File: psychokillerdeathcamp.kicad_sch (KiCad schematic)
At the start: 0 parts

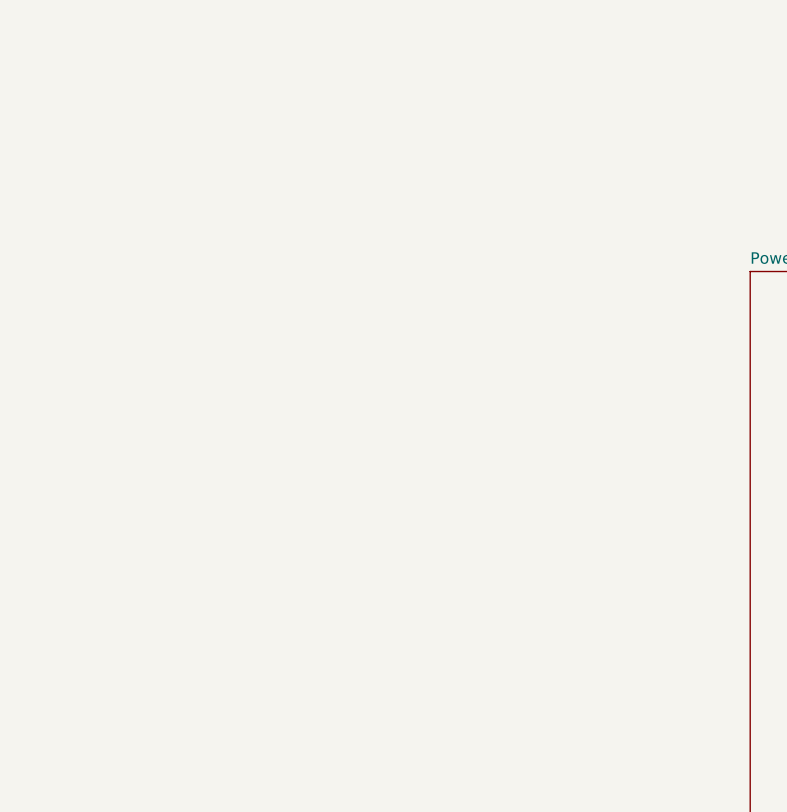
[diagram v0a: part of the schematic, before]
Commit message: fpga not done
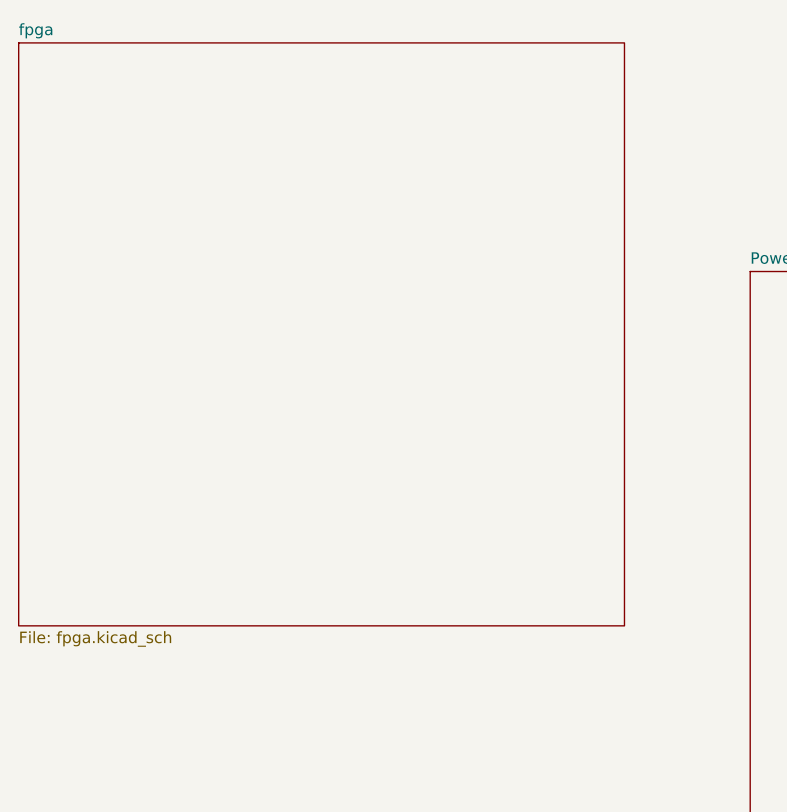
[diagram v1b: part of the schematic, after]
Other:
- added sheet fpga (fpga.kicad_sch)
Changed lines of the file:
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@@
+		)
+	)
+	(sheet
+		(at 19.05 38.1)
+		(size 67.31 64.77)
+		(exclude_from_sim no)
+		(in_bom yes)
+		(on_board yes)
+		(dnp no)
+		(fields_autoplaced yes)
+		(stroke
+			(width 0.1524)
+			(type solid)
+		)
+		(fill
+			(color 0 0 0 0)
+		)
+		(property "Sheetname" "fpga"
+			(at 19.05 37.3884 0)
+			(show_name no)
+			(do_not_autoplace no)
+			(effects
+				(font
+					(size 1.27 1.27)
+				)
+				(justify left bottom)
+			)
+		)
+		(property "Sheetfile" "fpga.kicad_sch"
+			(at 19.05 103.4546 0)
+			(show_name no)
+			(do_not_autoplace no)
+			(effects
+				(font
+					(size 1.27 1.27)
+				)
+				(justify left top)
+			)
+		)
+		(instances
+			(project "psychokillerdeathcamp"
+				(path "/bb761b47-4aa1-4d7a-b464-2f14c3f8c1bc"
+					(page "3")
+				)
+			)
 		)
 	)

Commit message: Add MCU file
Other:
- added sheet MCU (untitled.kicad_sch)
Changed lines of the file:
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@@
+	)
+	(sheet
+		(at 21.59 123.19)
+		(size 67.31 55.88)
+		(exclude_from_sim no)
+		(in_bom yes)
+		(on_board yes)
+		(dnp no)
+		(fields_autoplaced yes)
+		(stroke
+			(width 0.1524)
+			(type solid)
+		)
+		(fill
+			(color 0 0 0 0)
+		)
+		(property "Sheetname" "MCU"
+			(at 21.59 122.4784 0)
+			(show_name no)
+			(do_not_autoplace no)
+			(effects
+				(font
+					(size 1.27 1.27)
+				)
+				(justify left bottom)
+			)
+		)
+		(property "Sheetfile" "untitled.kicad_sch"
+			(at 21.59 179.6546 0)
+			(show_name no)
+			(do_not_autoplace no)
+			(effects
+				(font
+					(size 1.27 1.27)
+				)
+				(justify left top)
+			)
+		)
+		(instances
+			(project "psychokillerdeathcamp"
+				(path "/bb761b47-4aa1-4d7a-b464-2f14c3f8c1bc"
+					(page "4")
+				)
+			)
+		)
 	)
 	(sheet
